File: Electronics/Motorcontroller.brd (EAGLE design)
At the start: 100 x 48.2 mm, 27 parts, among them Q1 IRFZ48V, Q2 IRF4905V, Q3 IRFZ48V, Q4 IRF4905V, Q5 IRFZ48V, Q6 IRF4905V, Q7 IRFZ48V, Q8 IRF4905V, X3 24V Batt

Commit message: Motorboard v2.0
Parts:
- added LED2, LED3, LED4, LED5: (no value), led:LED3MM
- added R7, R8: 2.2k, rcl:0207/10
- LED1: device led:LED5MM -> led:LED3MM
- moved R6 10.4 mm to (87.0, 52.1), turned to 180 degrees
- moved R5 9.92 mm to (74.9, 52.1), turned to 180 degrees
- moved R2 9.44 mm to (37.5, 52.1), turned to 180 degrees
- moved R4 9.44 mm to (62.9, 52.1), turned to 180 degrees
- moved R1 8.98 mm to (25.4, 52.1), turned to 0 degrees
- moved R3 8.98 mm to (50.2, 52.1), turned to 0 degrees
- moved LED1 2.37 mm to (38.7, 68.2), turned to 90 degrees
- moved C1 2.29 mm to (63.2, 73.2)
- moved X1 2.01 mm to (23.5, 71.8)
- moved X2 2.01 mm to (76.8, 71.8)
- moved JP1 1.91 mm to (9.21, 42.9)
- moved OK1 1.91 mm to (25.4, 45.1)
- moved OK2 1.91 mm to (38.1, 45.1)
- moved OK3 1.91 mm to (50.8, 45.1)
- moved OK4 1.91 mm to (63.5, 45.1)
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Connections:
- removed net N$1: Q5.D, Q6.D, X2.2
- new net N$23: LED2.K, LED3.A, R7.2
- new net N$24: LED4.A, LED5.K, R8.2
- new net N$25: LED4.K, LED5.A, Q5.D, Q6.D, X2.2
- net N$18: now also R8.1
- net N$2: now also R7.1
- net N$4: now also LED2.A, LED3.K
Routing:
- net N$25: track 0.00 -> 71.1 mm, vias 0 -> 2
- net N$1: track 37.4 -> 0.00 mm
- net N$12: track 68.1 -> 32.6 mm, vias 2 -> 0
- net +24V: track 199.7 -> 170.5 mm, vias 2 -> 0
- net N$4: track 24.8 -> 53.8 mm
- net N$21: track 80.6 -> 66.3 mm, vias 1 -> 2
- net N$9: track 95.9 -> 106.1 mm
- net N$23: track 0.00 -> 9.15 mm
- net N$2: track 36.7 -> 44.5 mm
- net N$24: track 0.00 -> 7.51 mm
- net GND2: track 263.7 -> 258.9 mm
- net N$13: track 123.6 -> 126.6 mm, vias 1 -> 2
- net N$11: track 84.9 -> 86.6 mm
- net N$3: track 11.3 -> 9.76 mm
- net GND: track 102.6 -> 101.3 mm
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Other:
- board size 100 x 48.2 mm -> 101.3 x 50.8 mm
- board text added: "8 mar 2012"
- board text added: "Motorcontroller v2.0"
- board text removed: "24 jan 2012"
- board text removed: "Motorcontroller v1.0"

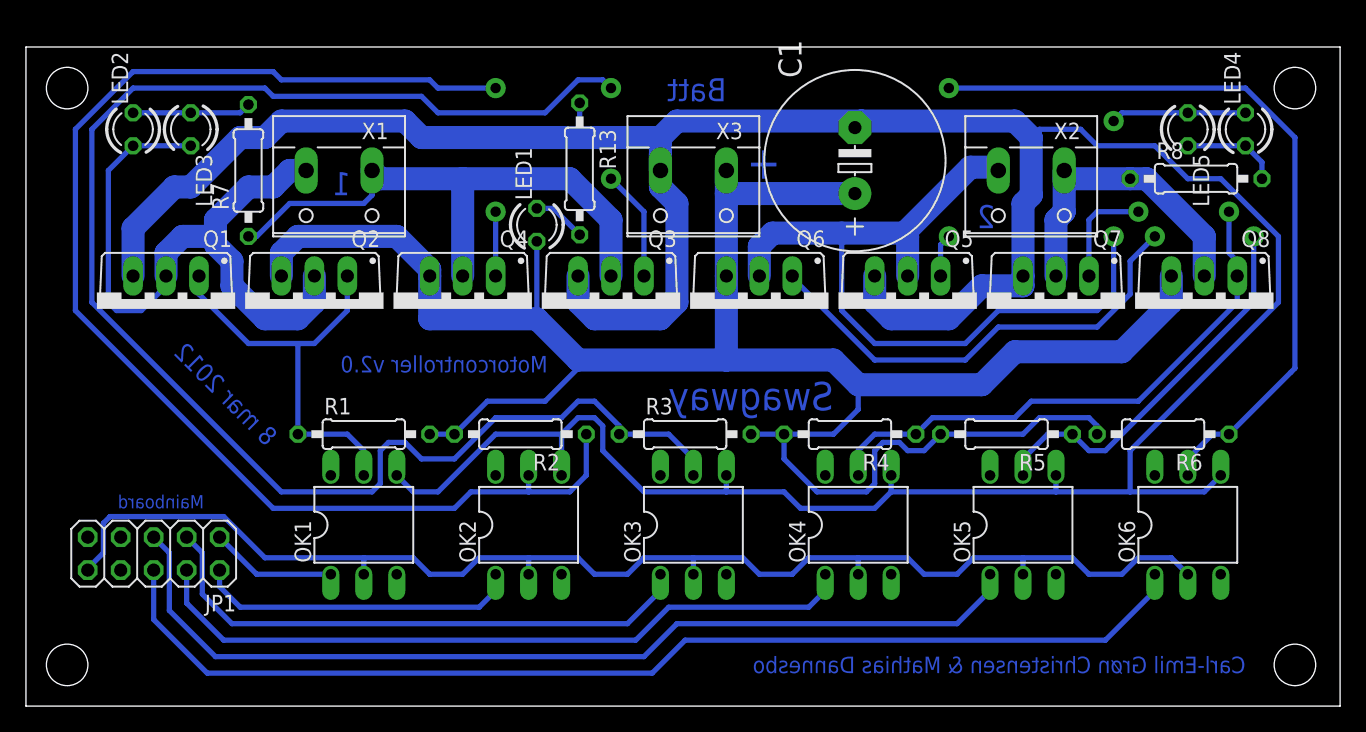
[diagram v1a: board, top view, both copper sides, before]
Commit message: Motorboard: pad sizes and small reroutes
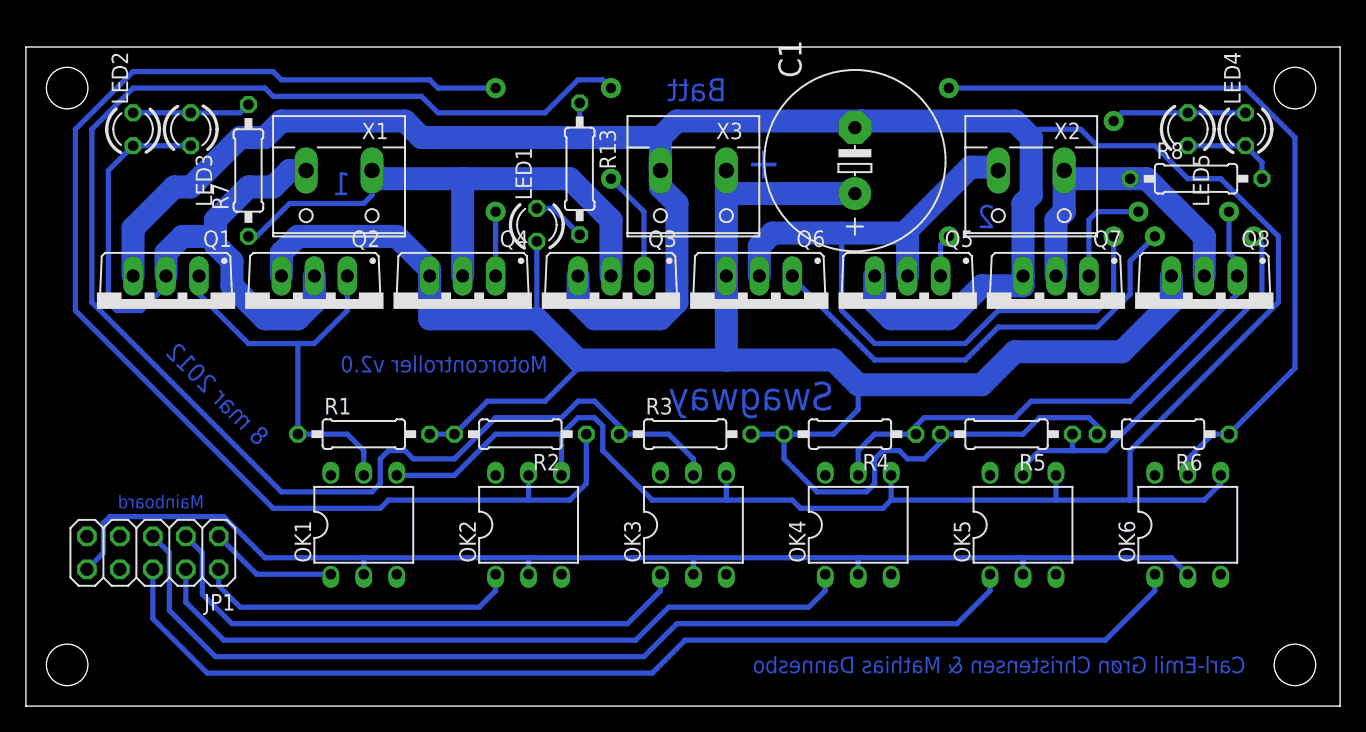
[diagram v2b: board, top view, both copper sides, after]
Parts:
- moved JP1 0.09 mm to (9.14, 42.9)
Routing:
- net GND: track 101.3 -> 96.0 mm
- net GND2: track 258.9 -> 260.7 mm
- net N$13: track 126.6 -> 125.7 mm

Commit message: Few proximity reroutes
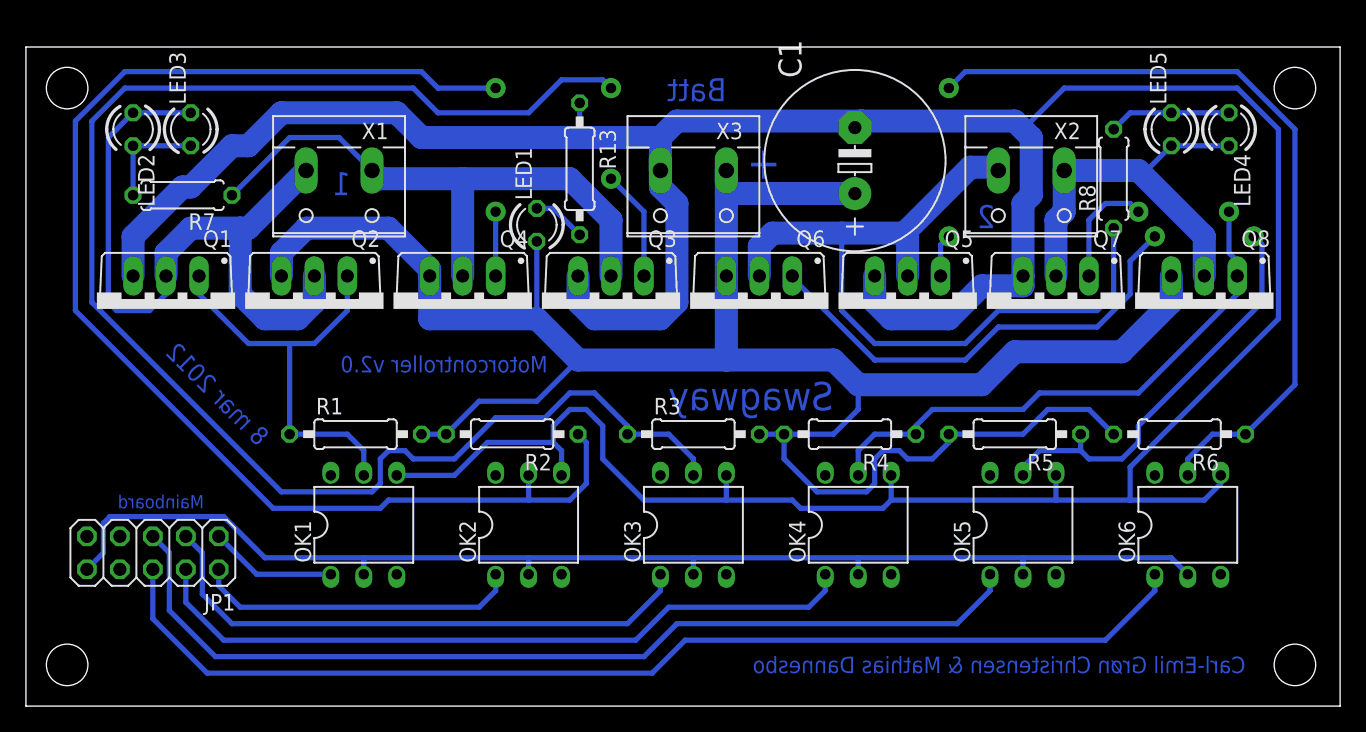
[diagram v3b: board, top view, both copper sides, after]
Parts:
- R7, R8: device rcl:0207/10 -> rcl:0207/7
- moved R8 6.35 mm to (83.2, 71.8), turned to 90 degrees
- moved R7 5.43 mm to (11.4, 70.5), turned to 180 degrees
- moved LED5 1.27 mm to (87.6, 75.6), turned to 90 degrees
- moved LED4 1.27 mm to (92.1, 75.6), turned to 270 degrees
- moved R6 1.27 mm to (88.3, 52.1)
- moved R2 0.64 mm to (36.8, 52.1)
- moved R1 0.63 mm to (24.8, 52.1)
- moved R3 0.63 mm to (50.8, 52.1)
- moved R5 0.63 mm to (75.6, 52.1)
- turned LED2 to 270 degrees
- turned LED3 to 90 degrees
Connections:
- removed net N$18: Q7.D, Q8.D, R8.1, X2.1
- new net N$1: LED4.K, LED5.A, Q7.D, Q8.D, X2.1
- net N$25: now also R8.1; no longer LED4.K, LED5.A
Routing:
- net N$1: track 0.00 -> 32.1 mm
- net N$18: track 24.1 -> 0.00 mm
- net N$25: track 71.1 -> 61.3 mm, vias 2 -> 0
- net GND2: track 260.7 -> 270.0 mm
- net +24V: track 170.5 -> 172.7 mm
- net N$22: track 61.8 -> 63.9 mm
- net N$4: track 53.8 -> 55.8 mm
- net N$24: track 7.51 -> 9.42 mm
- net N$21: track 66.7 -> 68.3 mm
- net N$2: track 44.5 -> 45.5 mm
- net N$13: track 125.7 -> 126.6 mm
- net N$23: track 9.15 -> 8.26 mm
- net N$9: track 105.9 -> 106.5 mm
- net N$12: track 32.6 -> 33.3 mm
- net N$19: track 51.6 -> 52.1 mm

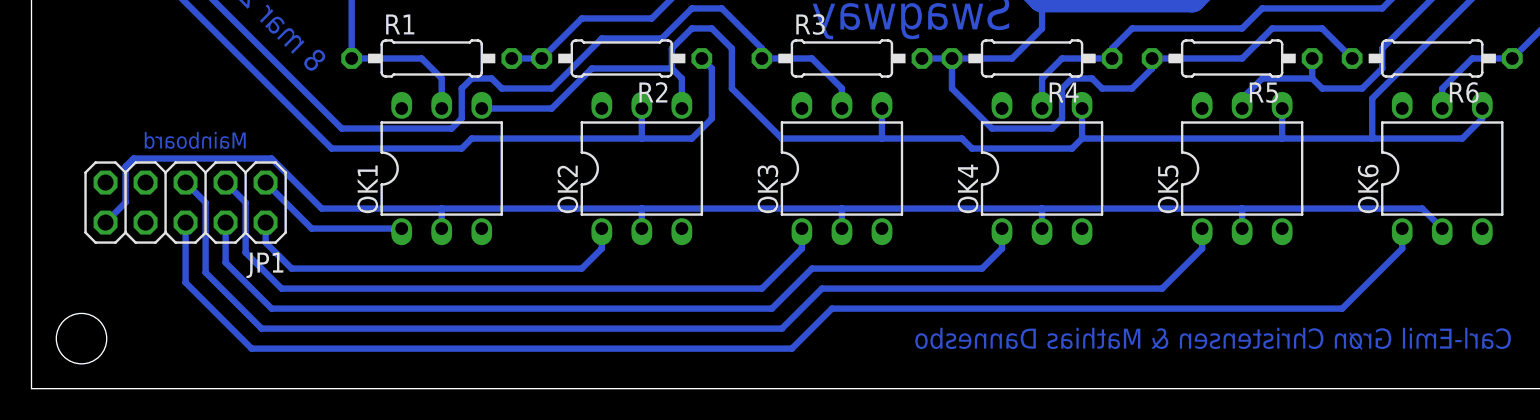
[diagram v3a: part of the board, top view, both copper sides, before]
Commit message: Reroute around header
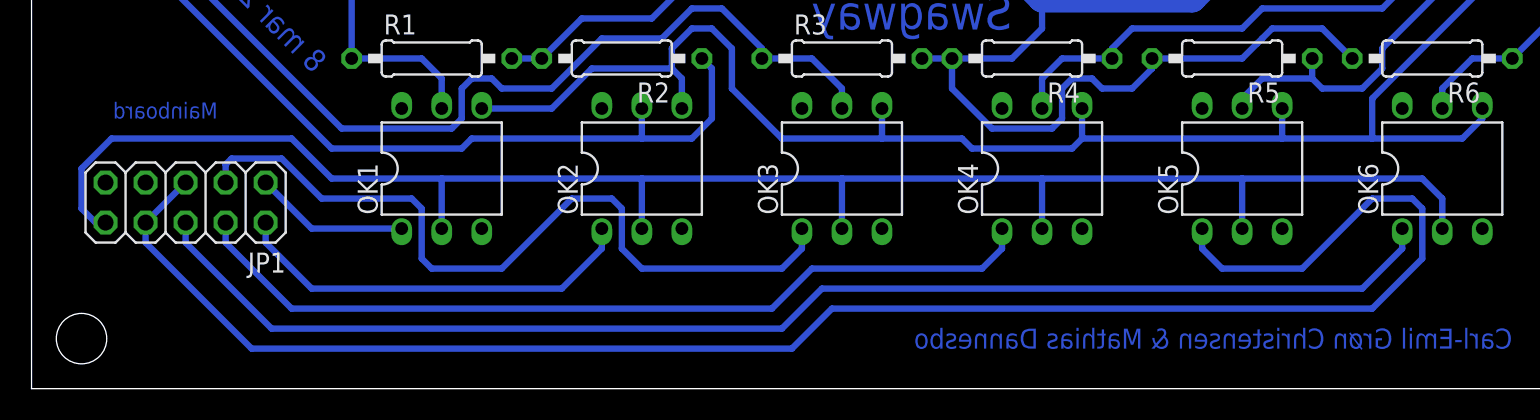
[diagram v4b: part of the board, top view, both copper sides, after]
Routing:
- net N$10: track 74.3 -> 112.1 mm
- net GND: track 96.0 -> 110.9 mm
- net N$7: track 43.5 -> 49.6 mm
- net N$11: track 86.7 -> 84.1 mm
- net N$5: track 25.1 -> 26.1 mm
- net N$8: track 55.9 -> 55.1 mm
